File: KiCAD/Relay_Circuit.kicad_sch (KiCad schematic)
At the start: 6 parts, among them K1 G5V-1, U2 PC365NJ0000F

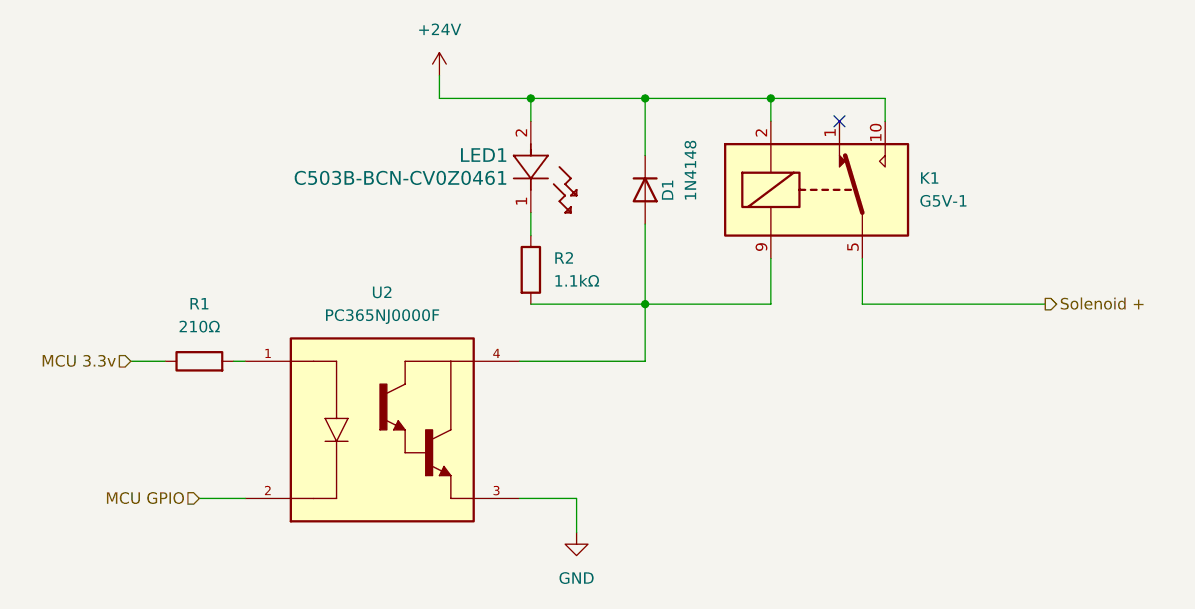
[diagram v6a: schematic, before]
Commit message: Replaced opto-isolator with through hole version
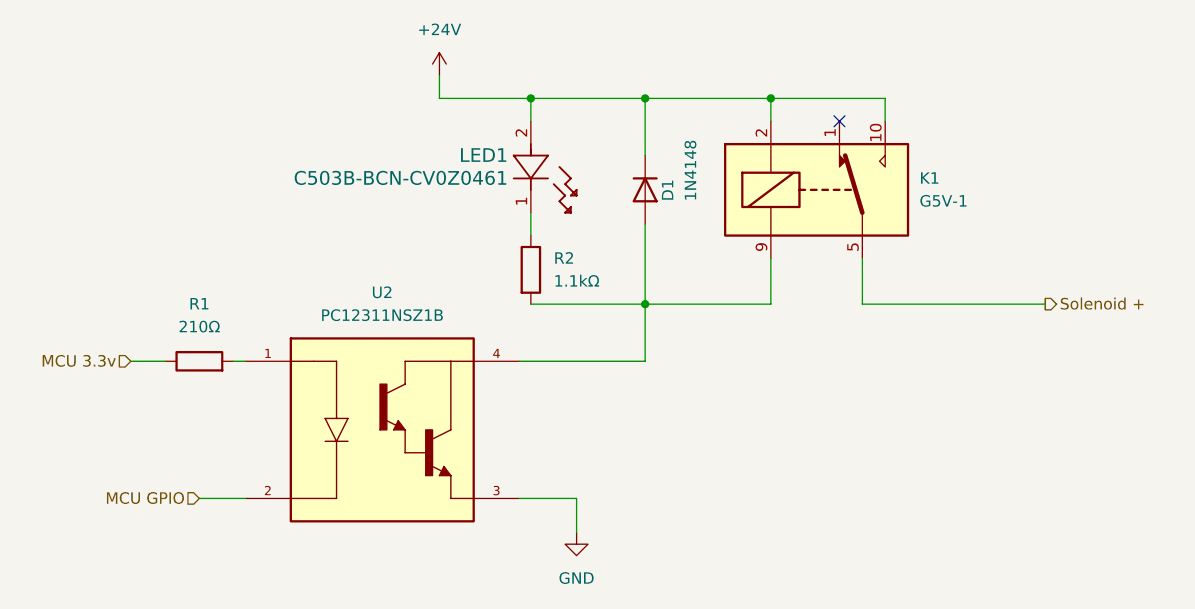
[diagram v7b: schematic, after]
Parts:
- removed U2: PC365NJ0000F, PC365NJ0000F:PC365NJ0000F, symbol PC365NJ0000F:PC365NJ0000F
- added U2: PC12311NSZ1B, PC12311NSZ1B:PC12311NSZ1B, symbol PC12311NSZ1B:PC12311NSZ1B
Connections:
- net GND: now also U2.3
- net MCU GPIO: now also U2.2
- net at D1.2 (A), K1.9, R2.2: now also U2.4
- net at R1.2: now also U2.1
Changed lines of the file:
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@@
+    )
+  )
+  (symbol (lib_id "PC12311NSZ1B:PC12311NSZ1B") (at 147.32 101.6 0) (unit 1)
+    (in_bom yes) (on_board yes) (dnp no) (fields_autoplaced)
+    (property "Reference" "U2" (at 146.05 85.09 0)
+      (effects (font (size 1.27 1.27)))
+    )
+    (property "Value" "PC12311NSZ1B" (at 146.05 87.63 0)
+      (effects (font (size 1.27 1.27)))
+    )
+    (property "Footprint" "PC12311NSZ1B:PC12311NSZ1B" (at 163.83 196.52 0)
+      (effects (font (size 1.27 1.27)) (justify left top) hide)
+    )
+    (property "Datasheet" "https://datasheet.datasheetarchive.com/originals/distributors/Datasheets_SAMA/562baaf804994183fb5e18c5f5c92935.pdf" (at 163.83 296.52 0)
+      (effects (font (size 1.27 1.27)) (justify left top) hide)
+    )
+    (property "Height" "4.45" (at 163.83 496.52 0)
+      (effects (font (size 1.27 1.27)) (justify left top) hide)
+    )
+    (property "Mouser Part Number" "852-PC12311NSZ1B" (at 163.83 596.52 0)
+      (effects (font (size 1.27 1.27)) (justify left top) hide)
+    )
+    (property "Mouser Price/Stock" "https://www.mouser.co.uk/ProductDetail/Sharp-Microelectronics/PC12311NSZ1B?qs=0lSvoLzn4L8JFTcuQxvmTA%3D%3D" (at 163.83 696.52 0)
+      (effects (font (size 1.27 1.27)) (justify left top) hide)
+    )
+    (property "Manufacturer_Name" "Sharp Microelectronics" (at 163.83 796.52 0)
+      (effects (font (size 1.27 1.27)) (justify left top) hide)
+    )
+    (property "Manufacturer_Part_Number" "PC12311NSZ1B" (at 163.83 896.52 0)
+      (effects (font (size 1.27 1.27)) (justify left top) hide)
+    )
+    (pin "1")
+    (pin "2")
+    (pin "3")
+    (pin "4")
+    (instances
+      (project "ColletAutoFeed_RelayBoard"
+        (path "/603d0a2e-fca7-40af-8fa8-51b59d823d4d/f85cc271-3b11-4af6-88e7-0089384d0a70"
+          (reference "U2") (unit 1)
+        )
+        (path "/603d0a2e-fca7-40af-8fa8-51b59d823d4d/1b4c4683-ae7a-43db-9c55-2e017b2b64f6"
+          (reference "U3") (unit 1)
+        )
+        (path "/603d0a2e-fca7-40af-8fa8-51b59d823d4d/c99ad83c-1e55-4897-95dc-696fc040ab27"
+          (reference "U4") (unit 1)
+        )
+        (path "/603d0a2e-fca7-40af-8fa8-51b59d823d4d/bf76bbb3-62c3-43bd-a097-b9f452e57b35"
+          (reference "U5") (unit 1)
+        )
+        (path "/603d0a2e-fca7-40af-8fa8-51b59d823d4d/c4c73976-bc86-4ae3-8f28-ea5e6a098449"
+          (reference "U6") (unit 1)
+        )
+        (path "/603d0a2e-fca7-40af-8fa8-51b59d823d4d/1e7f4279-2019-4687-9b9a-14c5bef026a1"
+          (reference "U7") (unit 1)
+        )
+        (path "/603d0a2e-fca7-40af-8fa8-51b59d823d4d/e9594ab2-eb4a-412d-b212-c8b9b51a6168"
+          (reference "U8") (unit 1)
+        )
+        (path "/603d0a2e-fca7-40af-8fa8-51b59d823d4d/b14b409f-5174-4f0c-b56e-0f620ad960f8"
+          (reference "U9") (unit 1)
+        )
+      )
     )
   )
@@
         )
       )
-    )
-  )
-  (symbol (lib_id "PC365NJ0000F:PC365NJ0000F") (at 146.05 100.33 0) (unit 1)
-    (in_bom yes) (on_board yes) (dnp no) (fields_autoplaced)
-    (property "Reference" "U2" (at 146.05 85.09 0)
-      (effects (font (size 1.27 1.27)))
-    )
-    (property "Value" "PC365NJ0000F" (at 146.05 87.63 0)
-      (effects (font (size 1.27 1.27)))
-    )
-    (property "Footprint" "PC365NJ0000F:PC365NJ0000F" (at 146.05 100.33 0)
-      (effects (font (size 1.27 1.27)) (justify bottom) hide)
-    )
-    (property "Datasheet" "" (at 146.05 100.33 0)
-      (effects (font (size 1.27 1.27)) hide)
-    )
-    (property "PARTREV" "Jun. 30. 2005" (at 146.05 100.33 0)
-      (effects (font (size 1.27 1.27)) (justify bottom) hide)
-    )
-    (property "MANUFACTURER" "Sharp" (at 146.05 100.33 0)
-      (effects (font (size 1.27 1.27)) (justify bottom) hide)
-    )
-    (property "MAXIMUM_PACKAGE_HEIGHT" "2.80mm" (at 146.05 100.33 0)
-      (effects (font (size 1.27 1.27)) (justify bottom) hide)
-    )
-    (property "STANDARD" "IPC-7351B" (at 146.05 100.33 0)
-      (effects (font (size 1.27 1.27)) (justify bottom) hide)
-    )
-    (pin "1")
-    (pin "2")
-    (pin "3")
-    (pin "4")
-    (instances
-      (project "ColletAutoFeed_RelayBoard"
-        (path "/603d0a2e-fca7-40af-8fa8-51b59d823d4d/f85cc271-3b11-4af6-88e7-0089384d0a70"
-          (reference "U2") (unit 1)
-        )
-        (path "/603d0a2e-fca7-40af-8fa8-51b59d823d4d/1b4c4683-ae7a-43db-9c55-2e017b2b64f6"
-          (reference "U3") (unit 1)
-        )
-        (path "/603d0a2e-fca7-40af-8fa8-51b59d823d4d/c99ad83c-1e55-4897-95dc-696fc040ab27"
-          (reference "U4") (unit 1)
-        )
-        (path "/603d0a2e-fca7-40af-8fa8-51b59d823d4d/bf76bbb3-62c3-43bd-a097-b9f452e57b35"
-          (reference "U5") (unit 1)
-        )
-        (path "/603d0a2e-fca7-40af-8fa8-51b59d823d4d/c4c73976-bc86-4ae3-8f28-ea5e6a098449"
-          (reference "U6") (unit 1)
-        )
-        (path "/603d0a2e-fca7-40af-8fa8-51b59d823d4d/1e7f4279-2019-4687-9b9a-14c5bef026a1"
-          (reference "U7") (unit 1)
-        )
-        (path "/603d0a2e-fca7-40af-8fa8-51b59d823d4d/e9594ab2-eb4a-412d-b212-c8b9b51a6168"
-          (reference "U8") (unit 1)
-        )
-        (path "/603d0a2e-fca7-40af-8fa8-51b59d823d4d/b14b409f-5174-4f0c-b56e-0f620ad960f8"
-          (reference "U9") (unit 1)
-        )
-      )
